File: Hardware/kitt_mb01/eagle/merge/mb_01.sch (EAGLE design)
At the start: 117 parts, among them CON1 ARDUINO_UNO, IC1.01 RT8293A, IC2.00 BQ24266RGET, IC3.01 LSM9DS1, J1 CON_HEADER_1X06-SMD-RIGHT-ANG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, J2 CON_HEADER_1X06-SMD-RIGHT-ANG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, P2 S2B-PH-K-S(LF)(SN), U1 MCP23017-E, U6.01 TPS61032RSARPSDO-G16, U7.01 SI1922EDH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

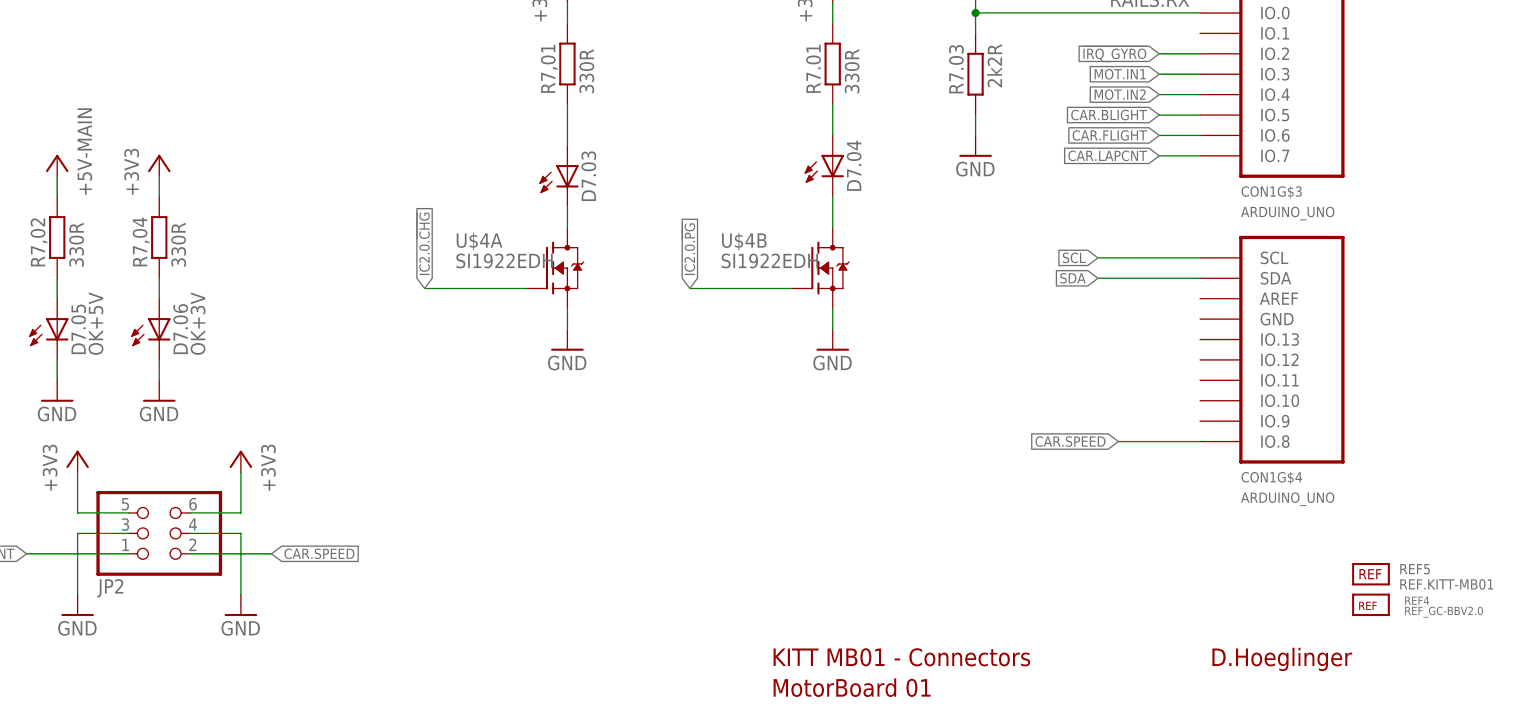
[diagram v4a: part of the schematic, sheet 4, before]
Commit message: added layer reference onto board
for the record: it's binary, because it needs less space
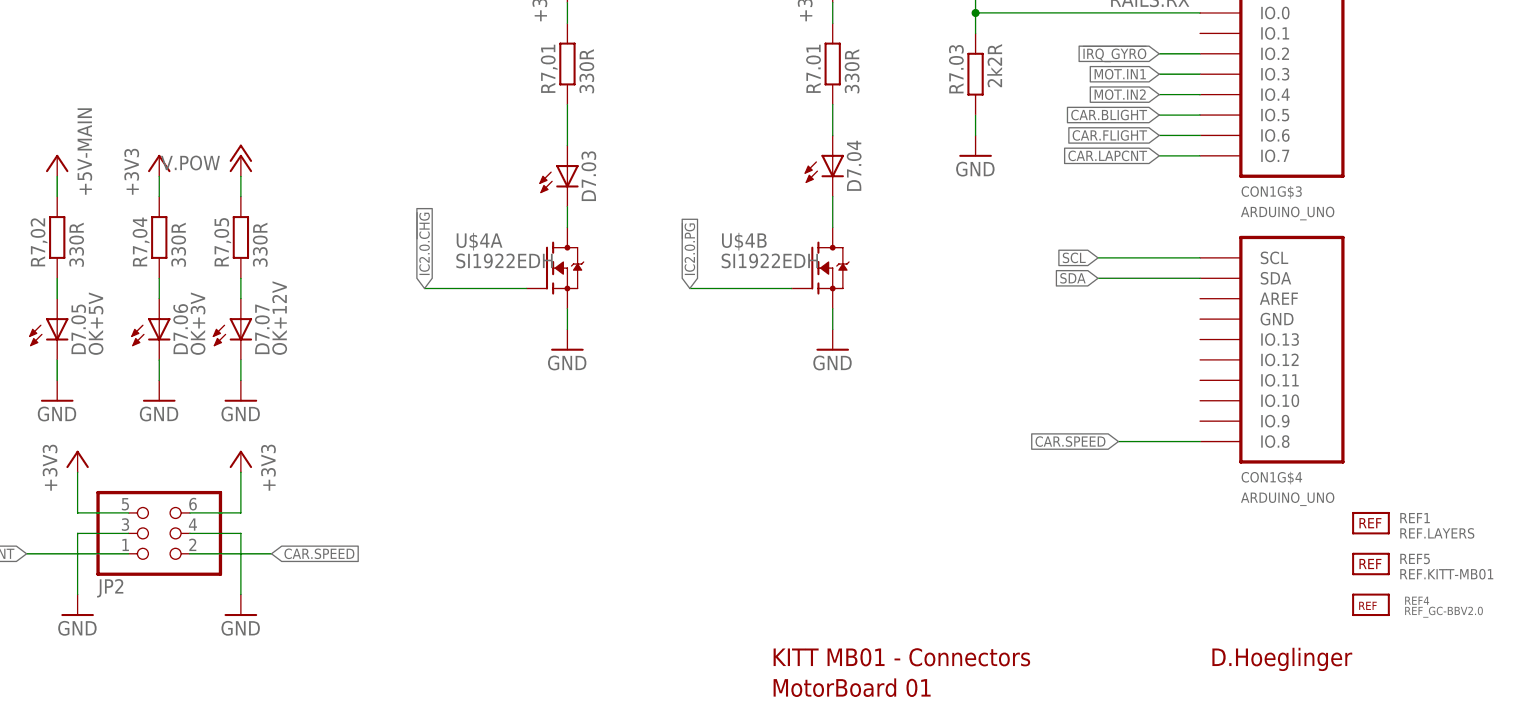
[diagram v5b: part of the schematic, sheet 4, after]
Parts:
- added D7.07: OK+12V, led:LEDCHIPLED_1206
- added R7,05: 330R, rcl:R-EU_R0603
- added REF1: REF.LAYERS, kitt.refs:REF.LAYERS
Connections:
- new net N$44: D7.07.A, R7,05.1
- net +12V: now also R7,05.2
- net GND: now also D7.07.C
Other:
- moved on the sheet: REF5
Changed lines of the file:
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@@
 <part name="J1" library="dp_devices" deviceset="CON_HEADER_1X06" device="-SMD-RIGHT-ANGLED"/>
 <part name="J2" library="dp_devices" deviceset="CON_HEADER_1X06" device="-SMD-RIGHT-ANGLED"/>
+<part name="P+5" library="supply1" deviceset="+12V" device="" value="V.POW"/>
+<part name="R7,05" library="rcl" deviceset="R-EU_" device="R0603" value="330R"/>
+<part name="D7.07" library="led" deviceset="LED" device="CHIPLED_1206" value="OK+12V"/>
+<part name="GND37" library="supply1" deviceset="GND" device=""/>
+<part name="REF1" library="kitt.refs" deviceset="REF.LAYERS" device=""/>
 </parts>
 <sheets>
@@
 <instance part="R7.03" gate="G$1" x="187.96" y="93.98" rot="MR270"/>
 <instance part="GND8" gate="1" x="187.96" y="83.82"/>
-<instance part="REF5" gate="G$1" x="234.95" y="30.48"/>
+<instance part="REF5" gate="G$1" x="234.95" y="31.75"/>
 <instance part="P+5VMAIN1" gate="1" x="27.94" y="167.64" rot="MR0"/>
 <instance part="X7.04" gate="-1" x="20.32" y="160.02" rot="MR0"/>
@@
 <instance part="J1" gate="J" x="-17.78" y="106.68" rot="R180"/>
 <instance part="J2" gate="J" x="-17.78" y="83.82" rot="R180"/>
+<instance part="P+5" gate="1" x="96.52" y="83.82" smashed="yes">
+<attribute name="VALUE" x="93.98" y="83.82" size="1.778" layer="96" rot="R180"/>
+</instance>
+<instance part="R7,05" gate="G$1" x="96.52" y="73.66" rot="R90"/>
+<instance part="D7.07" gate="G$1" x="96.52" y="63.5"/>
+<instance part="GND37" gate="1" x="96.52" y="53.34"/>
+<instance part="REF1" gate="G$1" x="234.95" y="36.83"/>
 </instances>
 <busses>
@@
 <wire x1="96.52" y1="36.83" x2="90.17" y2="36.83" width="0.1524" layer="91"/>
 </segment>
+<segment>
+<pinref part="GND37" gate="1" pin="GND"/>
+<pinref part="D7.07" gate="G$1" pin="C"/>
+<wire x1="96.52" y1="55.88" x2="96.52" y2="58.42" width="0.1524" layer="91"/>
+</segment>
 </net>
 <net name="RAILS.RX" class="0">
@@
 <pinref part="P+6" gate="1" pin="+12V"/>
 </segment>
+<segment>
+<pinref part="P+5" gate="1" pin="+12V"/>
+<pinref part="R7,05" gate="G$1" pin="2"/>
+<wire x1="96.52" y1="81.28" x2="96.52" y2="78.74" width="0.1524" layer="91"/>
+</segment>
 </net>
 <net name="SCL" class="0">
@@
 </segment>
 </net>
+<net name="N$44" class="0">
+<segment>
+<pinref part="D7.07" gate="G$1" pin="A"/>
+<pinref part="R7,05" gate="G$1" pin="1"/>
+<wire x1="96.52" y1="66.04" x2="96.52" y2="68.58" width="0.1524" layer="91"/>
+</segment>
+</net>

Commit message: snapshot of board merge : fancy pants edition -> added posh silk-screen logo    (possibly too large, still)
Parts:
- removed J1, J2: CON_HEADER_1X06-SMD-RIGHT-ANGLED, dp_devices:CON_HEADER_1X06-SMD-RIGHT-ANGLED
- removed JP3: (no value), pinhead:PINHD-1X18/90
- removed U1: MCP23017-E, kitt.ic:MCP23017-E
- added REF2: REF.LOGO.UASUA, kitt.refs:REF.LOGO.UASUA
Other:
- note removed: "TODO: PORT EXPANDER? Pro: +Utility +Knight Rider Effects Con: -More $€ -More routes"
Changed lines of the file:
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@@
 <part name="+3V12" library="supply1" deviceset="+3V3" device=""/>
 <part name="FRAME6" library="frames" deviceset="A4L-LOC" device=""/>
-<part name="FRAME7" library="frames" deviceset="A4L-LOC" device=""/>
-<part name="U1" library="kitt.ic" deviceset="MCP23017-E" device=""/>
 <part name="JP2" library="pinhead" deviceset="PINHD-2X3" device="/90"/>
 <part name="GND35" library="supply1" deviceset="GND" device=""/>
@@
 <part name="+3V14" library="supply1" deviceset="+3V3" device=""/>
 <part name="GND36" library="supply1" deviceset="GND" device=""/>
-<part name="JP3" library="pinhead" deviceset="PINHD-1X18" device="/90"/>
-<part name="J1" library="dp_devices" deviceset="CON_HEADER_1X06" device="-SMD-RIGHT-ANGLED"/>
-<part name="J2" library="dp_devices" deviceset="CON_HEADER_1X06" device="-SMD-RIGHT-ANGLED"/>
 <part name="P+5" library="supply1" deviceset="+12V" device="" value="V.POW"/>
 <part name="R7,05" library="rcl" deviceset="R-EU_" device="R0603" value="330R"/>
@@
 <part name="GND37" library="supply1" deviceset="GND" device=""/>
 <part name="REF1" library="kitt.refs" deviceset="REF.LAYERS" device=""/>
+<part name="REF2" library="kitt.refs" deviceset="REF.LOGO.UASUA" device=""/>
 </parts>
 <sheets>
@@
 <instance part="+3V14" gate="G$1" x="96.52" y="46.99" rot="MR0"/>
 <instance part="GND36" gate="1" x="96.52" y="26.67"/>
-<instance part="JP3" gate="A" x="-63.5" y="105.41"/>
-<instance part="J1" gate="J" x="-17.78" y="106.68" rot="R180"/>
-<instance part="J2" gate="J" x="-17.78" y="83.82" rot="R180"/>
 <instance part="P+5" gate="1" x="96.52" y="83.82" smashed="yes">
 <attribute name="VALUE" x="93.98" y="83.82" size="1.778" layer="96" rot="R180"/>
@@
 <instance part="GND37" gate="1" x="96.52" y="53.34"/>
 <instance part="REF1" gate="G$1" x="234.95" y="36.83"/>
+<instance part="REF2" gate="G$1" x="210.82" y="26.67"/>
 </instances>
 <busses>
@@
 </nets>
 </sheet>
-<sheet>
-<plain>
-<text x="99.06" y="50.8" size="1.778" layer="98">TODO:
-PORT EXPANDER?
-Pro: +Utility +Knight Rider Effects
-Con: -More $€ -More routes</text>
-</plain>
-<instances>
-<instance part="FRAME7" gate="G$1" x="0" y="0"/>
-<instance part="U1" gate="G$1" x="116.84" y="92.71"/>
-</instances>
-<busses>
-</busses>
-<nets>
-</nets>
-</sheet>

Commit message: added proper credits in schematics
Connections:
- new net ARDUINO.SCL: IC3.01.SCL/SPC
- new net ARDUINO.SDA: IC3.01.SDA/SDI/SDO
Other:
- note added: "D.Hoeglinger/A.Gessler"
- note added: "KITT MB01 - 5V Rail Power"
- note added: "KITT MB01 - Full Bridge Driver"
- note removed: "TODO: INTERNAL PULLUP OR WHAT?"
- moved on the sheet: C1.01, C1.02, C1.03, C1.04, C1.05, C1.06, C3.01, C3.02, C3.03, C3.04, C3.05, D1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

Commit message: snapshot of board merge
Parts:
- removed D7.01, D7.02: (no value), led:LEDCHIPLED_1206
- removed R7,03, R7.04: 330R, rcl:R-EU_R0603
- removed U$3: SI1922EDH, kitt.ic:SI1922EDH
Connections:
- removed net N$3: D7.01.C, U$3A.D
- removed net N$4: D7.01.A, R7,03.1
- removed net N$5: D7.02.A, R7.04.1
- removed net N$7: D7.02.C, U$3B.D
- net +3V3: no longer R7,03.2, R7.04.2
- net GND: no longer U$3A.S, U$3B.S
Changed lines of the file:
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@@
 <layer number="96" name="Values" color="7" fill="1" visible="yes" active="yes"/>
 <layer number="97" name="Info" color="7" fill="1" visible="yes" active="yes"/>
-<layer number="98" name="Guide" color="6" fill="1" visible="yes" active="yes"/>
+<layer number="98" name="Guide" color="6" fill="1" visible="no" active="yes"/>
 <layer number="99" name="SpiceOrder" color="5" fill="1" visible="yes" active="yes"/>
 <layer number="100" name="Muster" color="7" fill="1" visible="yes" active="yes"/>
@@
 <part name="SUPPLY4" library="supply2" deviceset="+4.1V" device="" value="VBAT+4.1V"/>
 <part name="R2.08" library="rcl" deviceset="R-EU_" device="R0402" value="[10kR/NTC]"/>
-<part name="P+5VMAIN2" library="supply1" deviceset="+5V" device="" value="+5V-MAIN"/>
 <part name="SUPPLY7" library="supply2" deviceset="+5V" device="" value="+5V-ALT"/>
 <part name="P+U2" library="supply1" deviceset="V+" device="" value="VDRV"/>
@@
 <part name="R0.01" library="rcl" deviceset="R-EU_" device="R1206" value="SHUNT"/>
 <part name="X7.02" library="con-phoenix-254" deviceset="MPT2" device="" value="HEAD-LIGHT"/>
-<part name="D7.01" library="led" deviceset="LED" device="CHIPLED_1206"/>
-<part name="U$3" library="kitt.ic" deviceset="SI1922EDH" device=""/>
-<part name="R7,03" library="rcl" deviceset="R-EU_" device="R0603" value="330R"/>
-<part name="R7.04" library="rcl" deviceset="R-EU_" device="R0603" value="330R"/>
-<part name="D7.02" library="led" deviceset="LED" device="CHIPLED_1206"/>
-<part name="GND26" library="supply1" deviceset="GND" device=""/>
-<part name="GND27" library="supply1" deviceset="GND" device=""/>
-<part name="+3V6" library="supply1" deviceset="+3V3" device=""/>
-<part name="+3V7" library="supply1" deviceset="+3V3" device=""/>
 <part name="GND28" library="supply1" deviceset="GND" device=""/>
 <part name="GND29" library="supply1" deviceset="GND" device=""/>
@@
 <instance part="SUPPLY4" gate="P" x="195.58" y="124.46"/>
 <instance part="R2.08" gate="G$1" x="198.12" y="55.88" rot="MR270"/>
-<instance part="P+5VMAIN2" gate="1" x="241.3" y="71.12" rot="MR0"/>
 <instance part="SUPPLY7" gate="+5V" x="33.02" y="149.86"/>
 <instance part="P+U2" gate="1" x="170.18" y="91.44"/>
@@
 Trainable Trackcars</text>
 <text x="163.83" y="15.24" size="2.1844" layer="94">MotorBoard 01</text>
+<text x="217.17" y="20.32" size="2.1844" layer="94">D.Hoeglinger</text>
 </plain>
 <instances>
@@
 <instance part="X7.02" gate="-1" x="21.59" y="102.87" rot="MR0"/>
 <instance part="X7.02" gate="-2" x="21.59" y="96.52" rot="MR0"/>
-<instance part="D7.01" gate="G$1" x="88.9" y="144.78"/>
-<instance part="U$3" gate="A" x="86.36" y="132.08"/>
-<instance part="U$3" gate="B" x="106.68" y="132.08"/>
-<instance part="R7,03" gate="G$1" x="88.9" y="157.48" rot="R90"/>
-<instance part="R7.04" gate="G$1" x="109.22" y="157.48" rot="R90"/>
-<instance part="D7.02" gate="G$1" x="109.22" y="146.05"/>
-<instance part="GND26" gate="1" x="88.9" y="121.92"/>
-<instance part="GND27" gate="1" x="109.22" y="121.92"/>
-<instance part="+3V6" gate="G$1" x="88.9" y="167.64"/>
-<instance part="+3V7" gate="G$1" x="109.22" y="167.64"/>
 <instance part="R0.01" gate="G$1" x="35.56" y="128.27"/>
 <instance part="GND28" gate="1" x="44.45" y="118.11"/>
@@
 </segment>
 <segment>
-<pinref part="U$3" gate="A" pin="S"/>
-<pinref part="GND26" gate="1" pin="GND"/>
-<wire x1="88.9" y1="127" x2="88.9" y2="124.46" width="0.1524" layer="91"/>
-</segment>
-<segment>
-<pinref part="U$3" gate="B" pin="S"/>
-<pinref part="GND27" gate="1" pin="GND"/>
-<wire x1="109.22" y1="127" x2="109.22" y2="124.46" width="0.1524" layer="91"/>
-</segment>
-<segment>
 <pinref part="GND28" gate="1" pin="GND"/>
 <wire x1="44.45" y1="120.65" x2="44.45" y2="128.27" width="0.1524" layer="91"/>
@@
 </segment>
 </net>
-<net name="N$3" class="0">
-<segment>
-<pinref part="D7.01" gate="G$1" pin="C"/>
-<pinref part="U$3" gate="A" pin="D"/>
-<wire x1="88.9" y1="139.7" x2="88.9" y2="137.16" width="0.1524" layer="91"/>
-</segment>
-</net>
-<net name="N$4" class="0">
-<segment>
-<pinref part="R7,03" gate="G$1" pin="1"/>
-<pinref part="D7.01" gate="G$1" pin="A"/>
-<wire x1="88.9" y1="152.4" x2="88.9" y2="147.32" width="0.1524" layer="91"/>
-</segment>
-</net>
-<net name="N$5" class="0">
-<segment>
-<pinref part="R7.04" gate="G$1" pin="1"/>
-<pinref part="D7.02" gate="G$1" pin="A"/>
-<wire x1="109.22" y1="152.4" x2="109.22" y2="148.59" width="0.1524" layer="91"/>
-</segment>
-</net>
-<net name="N$7" class="0">
-<segment>
-<pinref part="D7.02" gate="G$1" pin="C"/>
-<pinref part="U$3" gate="B" pin="D"/>
-<wire x1="109.22" y1="140.97" x2="109.22" y2="137.16" width="0.1524" layer="91"/>
-</segment>
-</net>
 <net name="+3V3" class="0">
 <segment>
-<pinref part="+3V7" gate="G$1" pin="+3V3"/>
-<pinref part="R7.04" gate="G$1" pin="2"/>
-<wire x1="109.22" y1="165.1" x2="109.22" y2="162.56" width="0.1524" layer="91"/>
-</segment>
-<segment>
-<pinref part="+3V6" gate="G$1" pin="+3V3"/>
-<pinref part="R7,03" gate="G$1" pin="2"/>
-<wire x1="88.9" y1="165.1" x2="88.9" y2="162.56" width="0.1524" layer="91"/>
-</segment>
-<segment>
 <pinref part="+3V9" gate="G$1" pin="+3V3"/>
